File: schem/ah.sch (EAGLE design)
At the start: 16 parts, among them IC1 74163N, IC10 74HC244N, IC11 74HC244N, IC12 74HC244N, IC13 74HC154N, IC14 74HC154N, IC15 74HC377N, IC16 74HC244N, IC2 74163N, IC3 74HC244N, IC4 74HC138N, IC5 74HC244N, IC6 74HC244N, IC7 74HC244N, IC8 74HC244N, IC9 74HC377N

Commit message: progress
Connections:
- removed net OBD0: IC14A.0
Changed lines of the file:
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@@
-</segment>
-</net>
-<net name="OBD0" class="0">
-<segment>
-<pinref part="IC14" gate="A" pin="0"/>
-<wire x1="101.6" y1="-71.12" x2="109.22" y2="-71.12" width="0.1524" layer="91"/>
-<label x="101.6" y="-71.12" size="1.778" layer="95"/>
 </segment>
 </net>

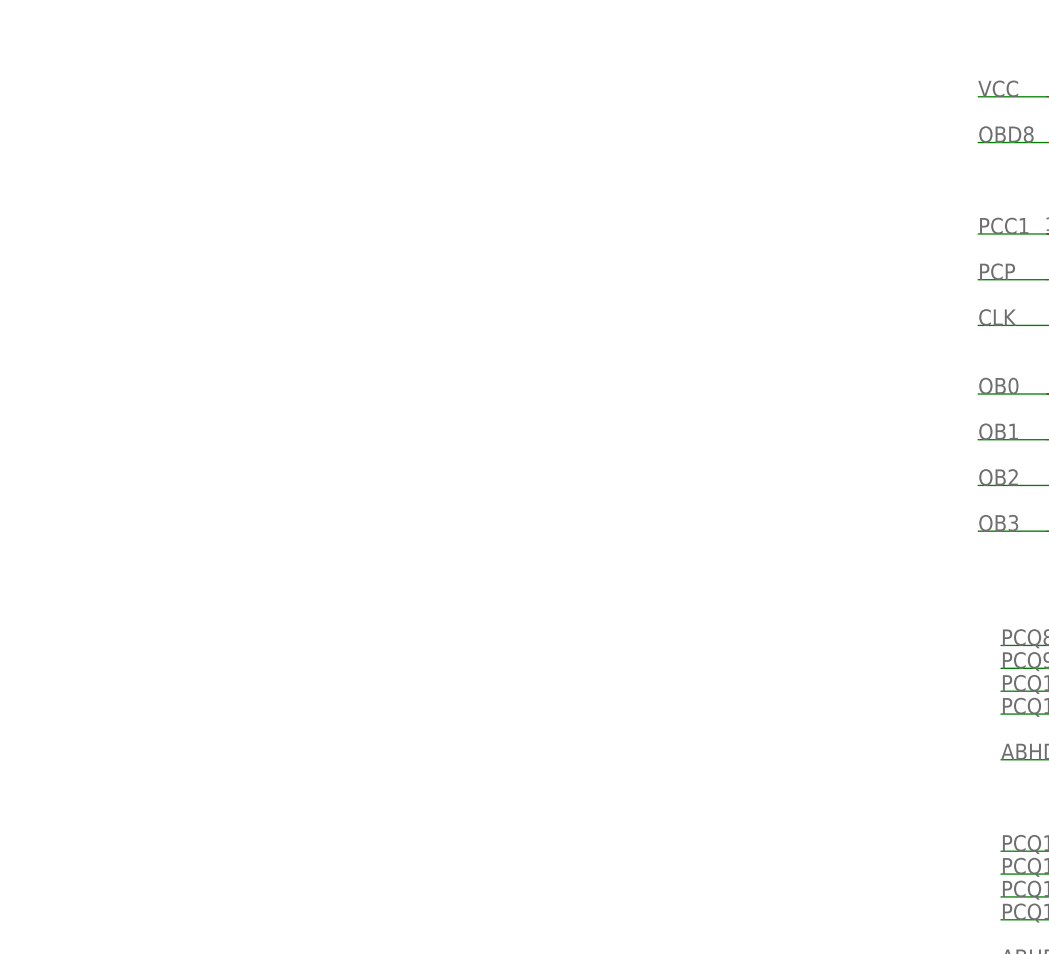
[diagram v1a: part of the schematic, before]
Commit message: finished most schematics
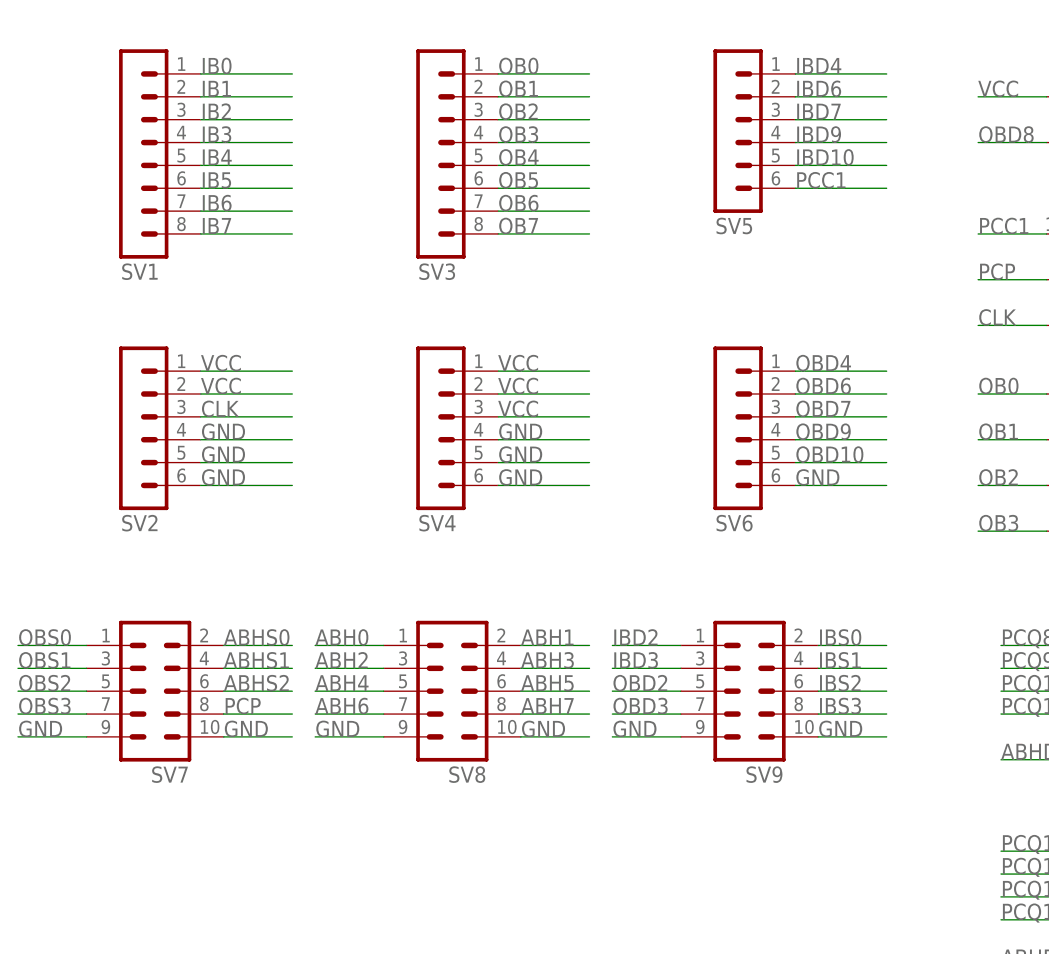
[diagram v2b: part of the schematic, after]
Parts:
- added SV1, SV3: (no value), con-lstb:MA08-1
- added SV2, SV4, SV5, SV6: (no value), con-lstb:MA06-1
- added SV7, SV8, SV9: (no value), con-lstb:MA05-2
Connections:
- net ABH0: now also SV8.1
- net ABH1: now also SV8.2
- net ABH2: now also SV8.3
- net ABH3: now also SV8.4
- net ABH4: now also SV8.5
- net ABH5: now also SV8.6
- net ABH6: now also SV8.7
- net ABH7: now also SV8.8
- net ABHS0: now also SV7.2
- net ABHS1: now also SV7.4
- net ABHS2: now also SV7.6
- net CLK: now also SV2.3
- net GND: now also SV2.4, SV2.5, SV2.6, SV4.4, SV4.5, SV4.6, SV6.6, SV7.10, SV7.9, SV8.10, SV8.9, SV9.10, SV9.9
- net IB0: now also SV1.1
- net IB1: now also SV1.2
- net IB2: now also SV1.3
- net IB3: now also SV1.4
- net IB4: now also SV1.5
- net IB5: now also SV1.6
- net IB6: now also SV1.7
- net IB7: now also SV1.8
- net IBD10: now also SV5.5
- net IBD2: now also SV9.1
- net IBD3: now also SV9.3
- net IBD4: now also SV5.1
- net IBD6: now also SV5.2
- net IBD7: now also SV5.3
- net IBD9: now also SV5.4
- net IBS0: now also SV9.2
- net IBS1: now also SV9.4
- net IBS2: now also SV9.6
- net IBS3: now also SV9.8
- net OB0: now also SV3.1
- net OB1: now also SV3.2
- net OB2: now also SV3.3
- net OB3: now also SV3.4
- net OB4: now also SV3.5
- net OB5: now also SV3.6
- net OB6: now also SV3.7
- net OB7: now also SV3.8
- net OBD10: now also SV6.5
- net OBD2: now also SV9.5
- net OBD3: now also SV9.7
- net OBD4: now also SV6.1
- net OBD6: now also SV6.2
- net OBD7: now also SV6.3
- net OBD9: now also SV6.4
- net OBS0: now also SV7.1
- net OBS1: now also SV7.3
- net OBS2: now also SV7.5
- net OBS3: now also SV7.7
- net PCC1: now also SV5.6
- net PCP: now also SV7.8
- net VCC: now also SV2.1, SV2.2, SV4.1, SV4.2, SV4.3

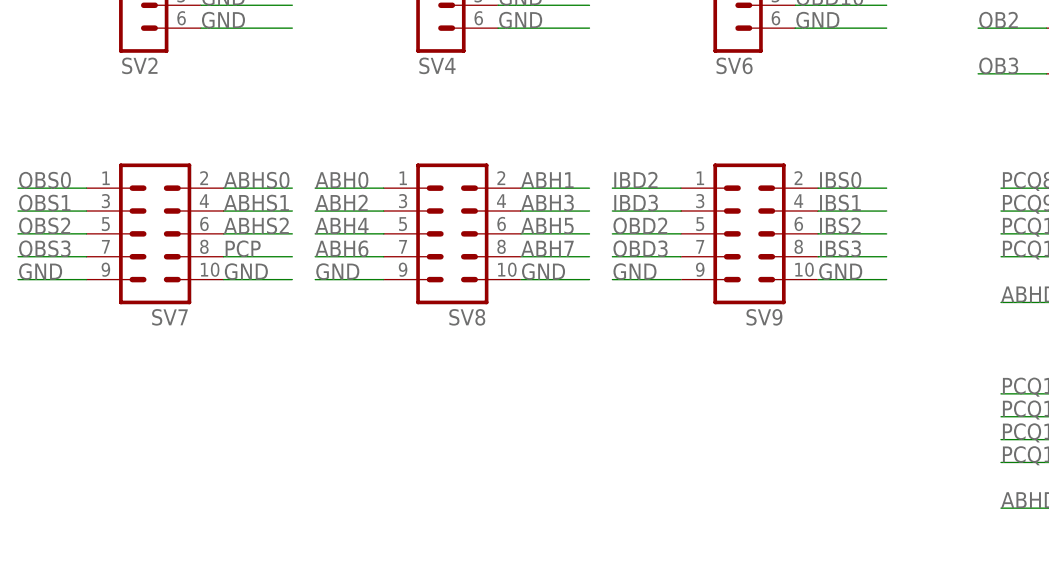
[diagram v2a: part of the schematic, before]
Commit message: adapted schematics for single headers
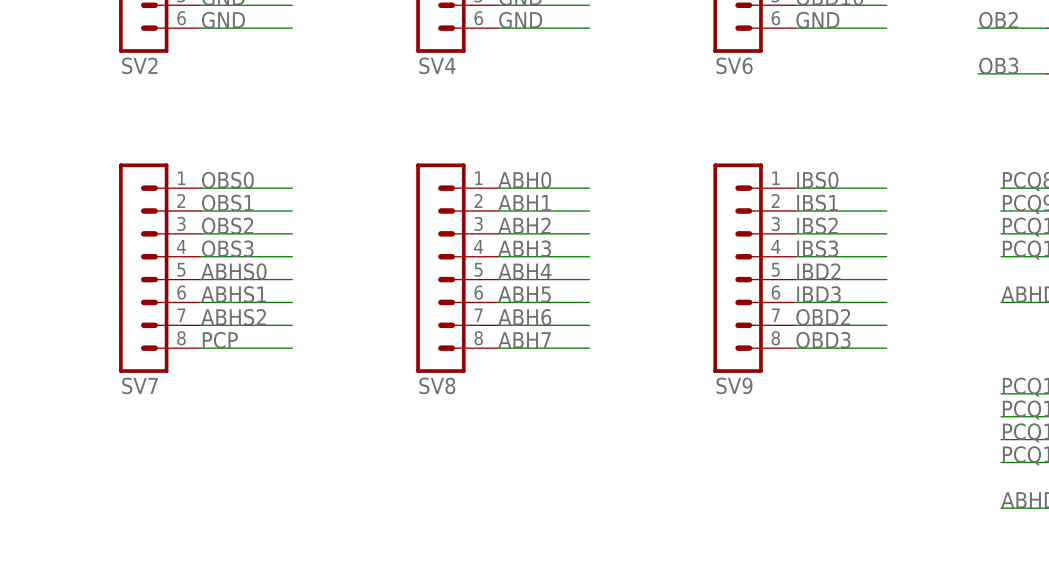
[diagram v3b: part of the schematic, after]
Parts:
- SV7, SV8, SV9: device con-lstb:MA05-2 -> con-lstb:MA08-1
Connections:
- net ABHS0: now also SV7.5; no longer SV7.2
- net ABHS1: now also SV7.6; no longer SV7.4
- net ABHS2: now also SV7.7; no longer SV7.6
- net GND: no longer SV7.10, SV7.9, SV8.10, SV8.9, SV9.10, SV9.9
- net IBD2: now also SV9.5; no longer SV9.1
- net IBD3: now also SV9.6; no longer SV9.3
- net IBS0: now also SV9.1; no longer SV9.2
- net IBS1: now also SV9.2; no longer SV9.4
- net IBS2: now also SV9.3; no longer SV9.6
- net IBS3: now also SV9.4; no longer SV9.8
- net OBD2: now also SV9.7; no longer SV9.5
- net OBD3: now also SV9.8; no longer SV9.7
- net OBS1: now also SV7.2; no longer SV7.3
- net OBS2: now also SV7.3; no longer SV7.5
- net OBS3: now also SV7.4; no longer SV7.7
